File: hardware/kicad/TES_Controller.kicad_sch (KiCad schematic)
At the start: 81 parts, among them CN1 B2PS-VH, CN2 S4B-XH-A, CN3 DG381-3.5-02P-14-00A, CN5 DG381-3.5-02P-14-00A, CN6 DG381-3.5-02P-14-00A, Q1 AO3400A, Q2 AO3400A, Q3 AO3400A, Q4 AO3401A, U1 ESP32-S3-WROOM-1, U10 DG301-5.0-02P-14-00A, U12 TJA1051T_3_1J, U5 ADS1115IDGSR, U6 AMS1117-3.3, U8 LMZM23601V5SILR

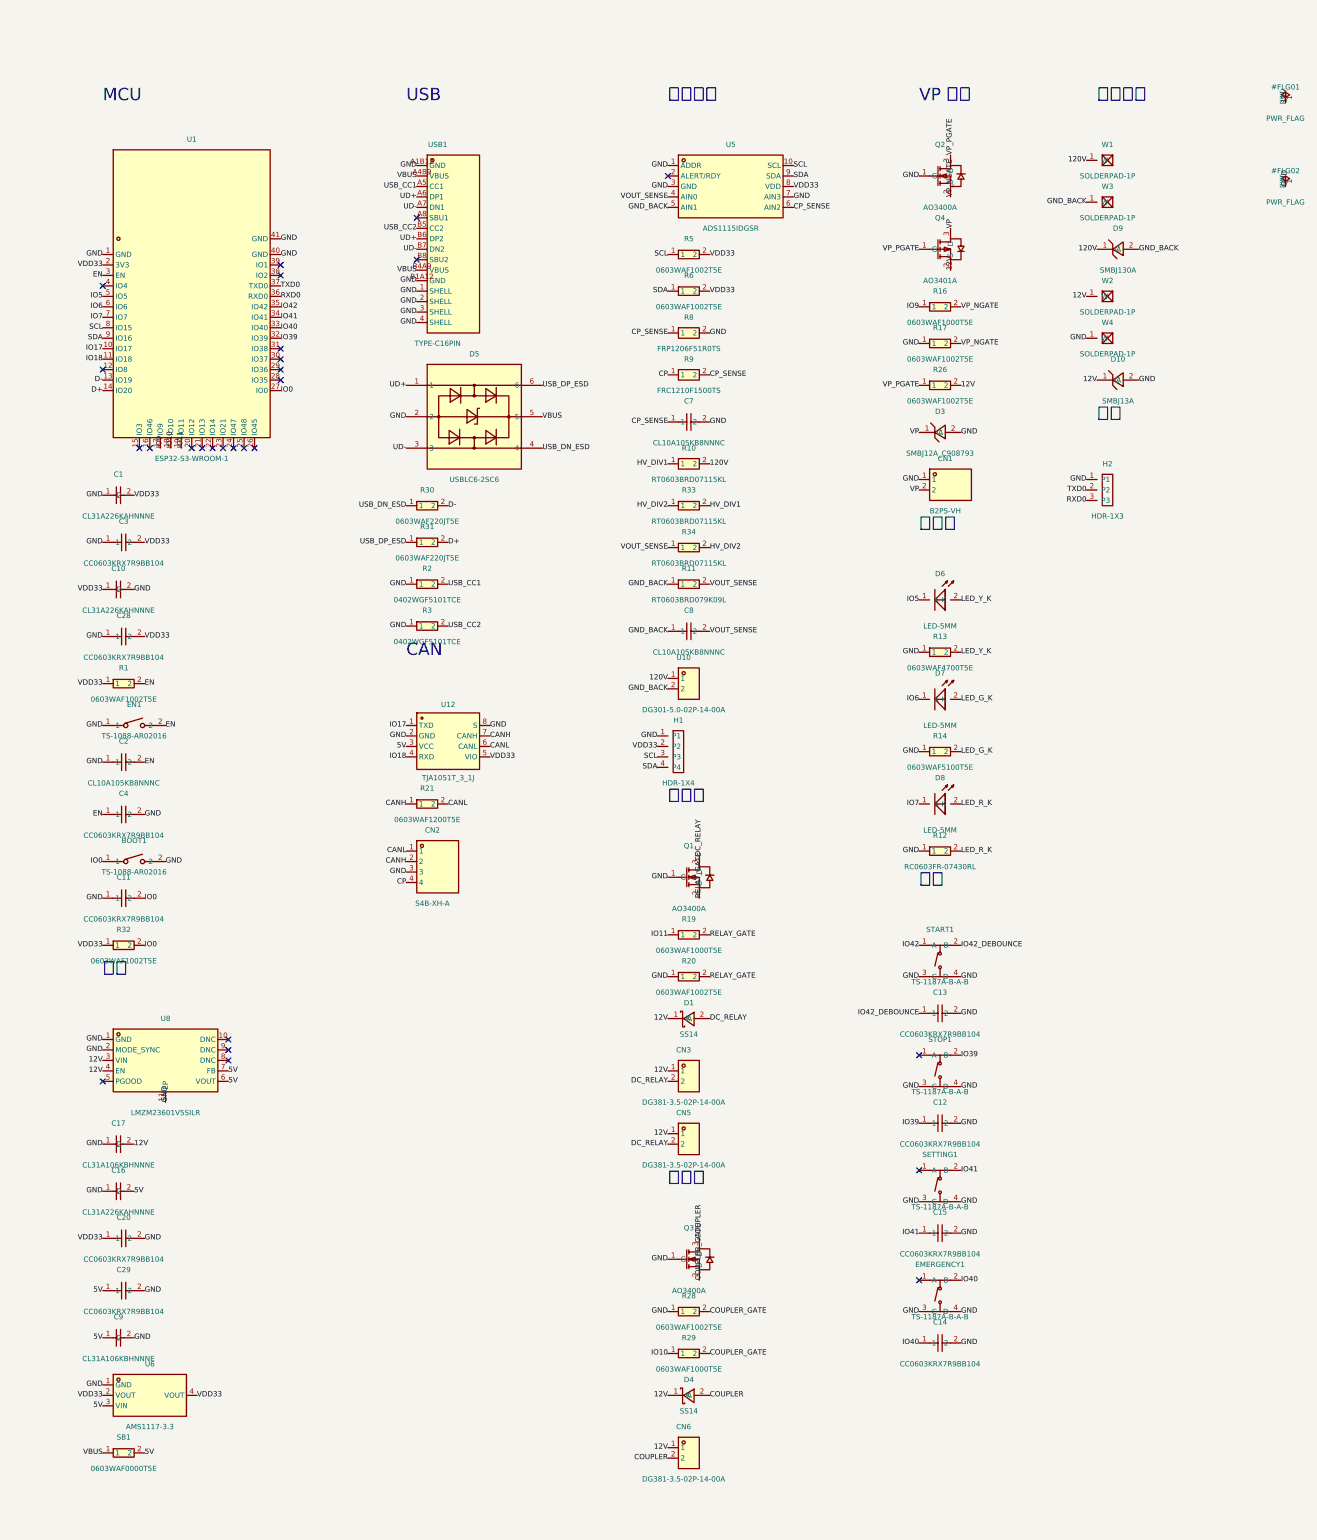
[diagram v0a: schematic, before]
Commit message: Draw the schematic with ground symbols and wires, not only labels
Chris found the schematic hard to read, and he is right: every pin carried a
net label and nothing was drawn as a connection, so a series chain looked
like three unrelated resistors sitting near each other. That was the cost of
generating it — 253 connections verified against the source, none of them
legible.

Two changes get most of it back.

Ground and supply pins become symbols instead of labels. Of 238 labels, 114
were power nets and 73 of those were GND alone; "this pin goes to ground" is
now a shape rather than a word. GND and GND_BACK are drawn differently on
purpose — the 120 V return is a separate node on the board, joined only
through the module's wiring, and one symbol for both would say otherwise.

Series chains are detected and laid out in a row with real wires between
them: the divider R34-R33-R10 and the three LED-and-resistor pairs. Chain
order comes from which side each pin sits on, so every link is a straight
horizontal line — the divider is detected as R10-R33-R34 but drawn in
reverse, because R10's connection is on its left.

Labels 232 to 119, with 115 wires and 110 power symbols.

Three things that had to be got right:

- Power symbols must be named exactly as the nets are. KiCad takes the net
  name from the symbol, so calling one +12V renames the whole net and the
  board's netlist with it.
- The stub between pin and symbol runs outward along the pin, not downward.
  At 2.54 mm it equals the symbol pin pitch, so a downward stub landed on
  the neighbouring pin and wired three no-connect pins to +12V.
- Wiring a net does not remove the need for a label on it. Dropping both
  left KiCad to auto-name the node Net-(R10-Pad1), which no longer matches
  HV_DIV1 on the board. One label per wired net keeps the name.

Netlist still verifies at 230 connections with zero difference, ERC clean,
and the board is untouched.

Co-Authored-By: Claude Opus 5 <noreply@anthropic.com>
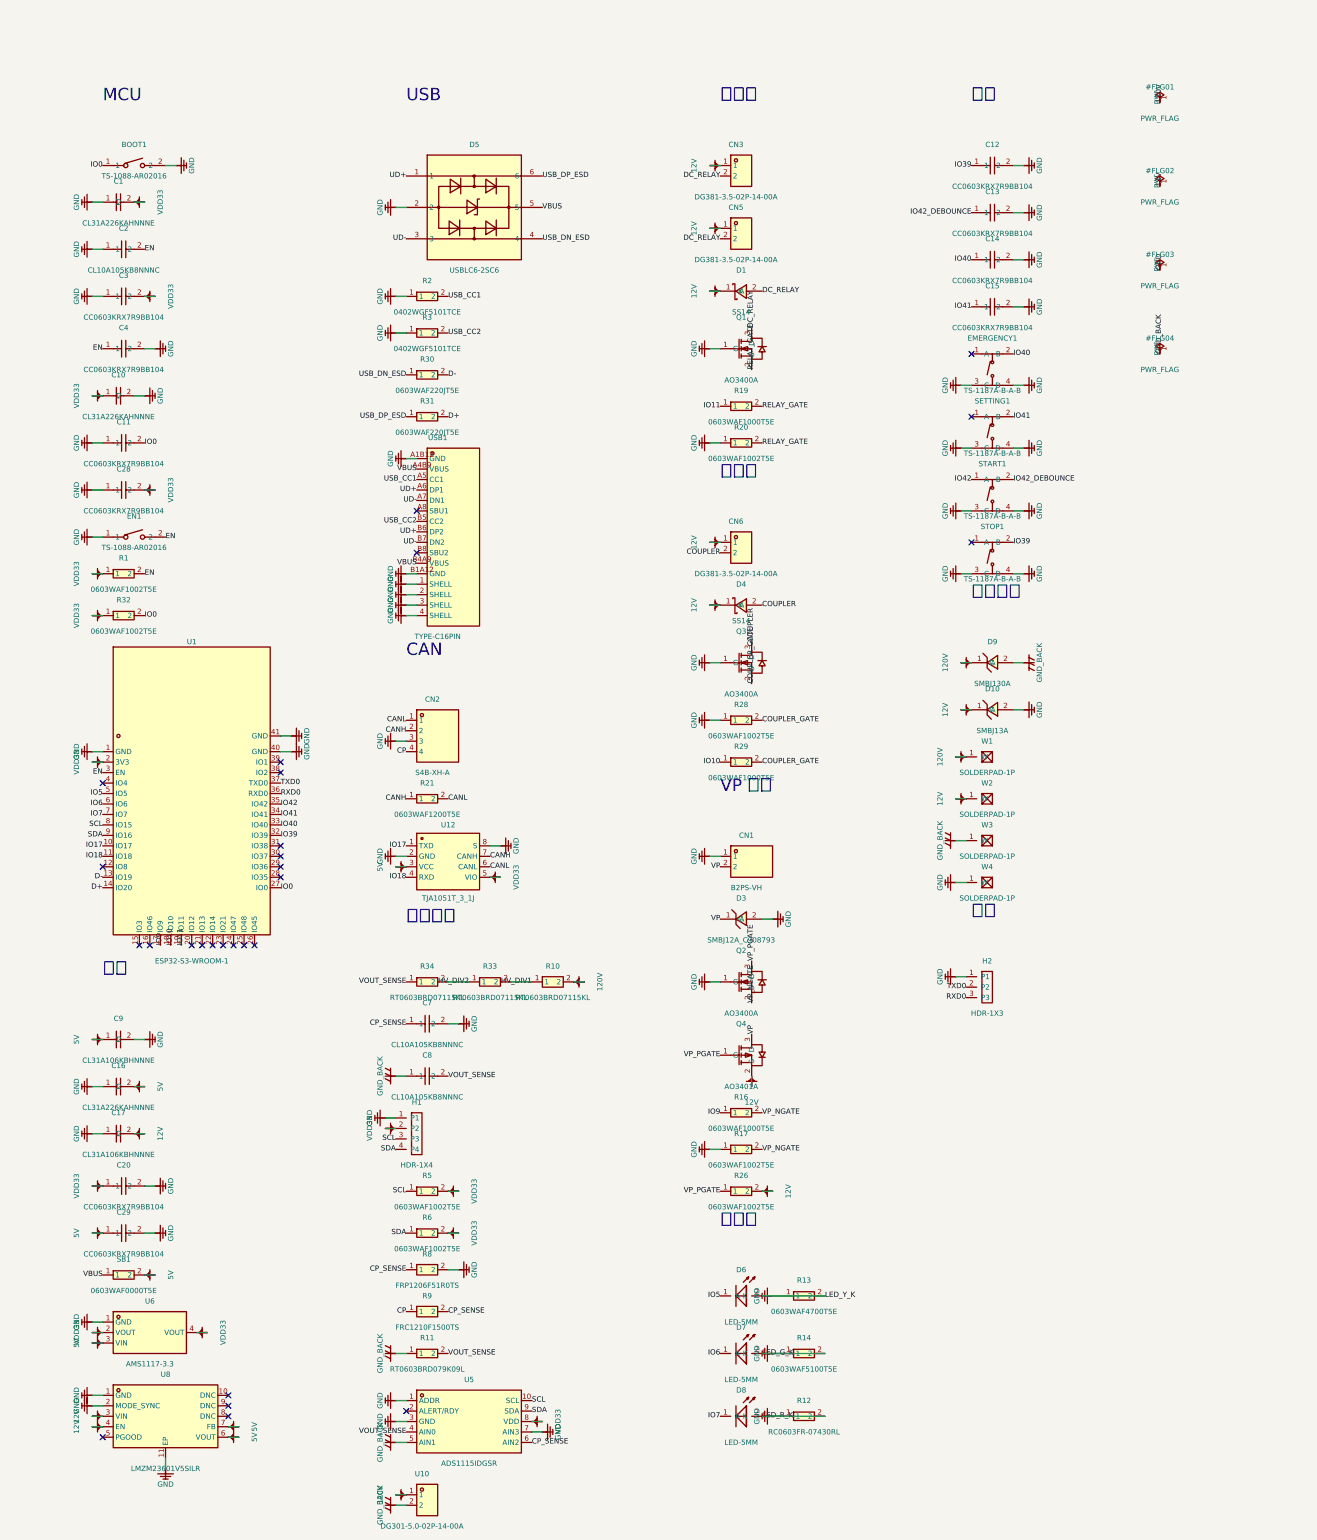
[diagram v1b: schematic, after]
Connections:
- net LED_G_K is gone; now on net GND: D7.2 (K), R14.2
- net LED_R_K is gone; now on net GND: D8.2 (K), R12.2
- net LED_Y_K is gone; now on net GND: D6.2 (K), R13.2

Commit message: Redraw the schematic the way it was drawn in EasyEDA
The generated schematic was correct but unreadable — everything was
arranged by the generator, so nothing sat where the author left it.
This rebuilds it from the original .esch: the same 73 components at the
same coordinates, the same 12 block titles and grouping boxes, the same
wires.

Getting the pins to land took working out what easyeda2kicad actually
does, which is: nothing. It copies EasyEDA's pin coordinates straight
into the KiCad symbol library, and KiCad's library Y axis points the
other way — so every symbol comes out upside down. tools/easyeda_symbols.py
checks this pin by pin against the original project file (25 of 25
symbols match with Y untouched, none negated), and the fix is to place
each symbol mirrored and rotated 180° + its original angle. KiCad
rotates before it mirrors; assuming the other order silently swaps pads
1 and 2 on every part rotated 90°, which reads as a plausible netlist.

Two things the original drawing does not tell you, both found by
comparing against the netlist rather than by eye:

* The library symbol is not always the symbol that was drawn. Q1-Q3 use
  AO3400A-MS, whose pins 1 and 2 are the reverse of the AO3400A the BOM
  points at. Wire matching now uses the symbol from the drawing, and
  components whose two geometries disagree (15 of them) are wired by
  label instead — the wires would otherwise attach to the wrong pin
  number and look fine.
* A wire group that grazes one pin of a neighbouring net used to be
  named alphabetically, so R10's move to HV_DIV1 renamed the whole
  divider midpoint. It is a majority vote now.

R10 also had to move: its pin 1 sat exactly on C8 pin 2, and once V1.3
separates those nets, cutting the wire is not enough — two labels at one
coordinate is still one node.

Netlist verifies at zero difference against the EasyEDA export (230 of
230 connections), ERC is clean, and the PCB is untouched (0 DRC errors,
0 unconnected).

Co-Authored-By: Cl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
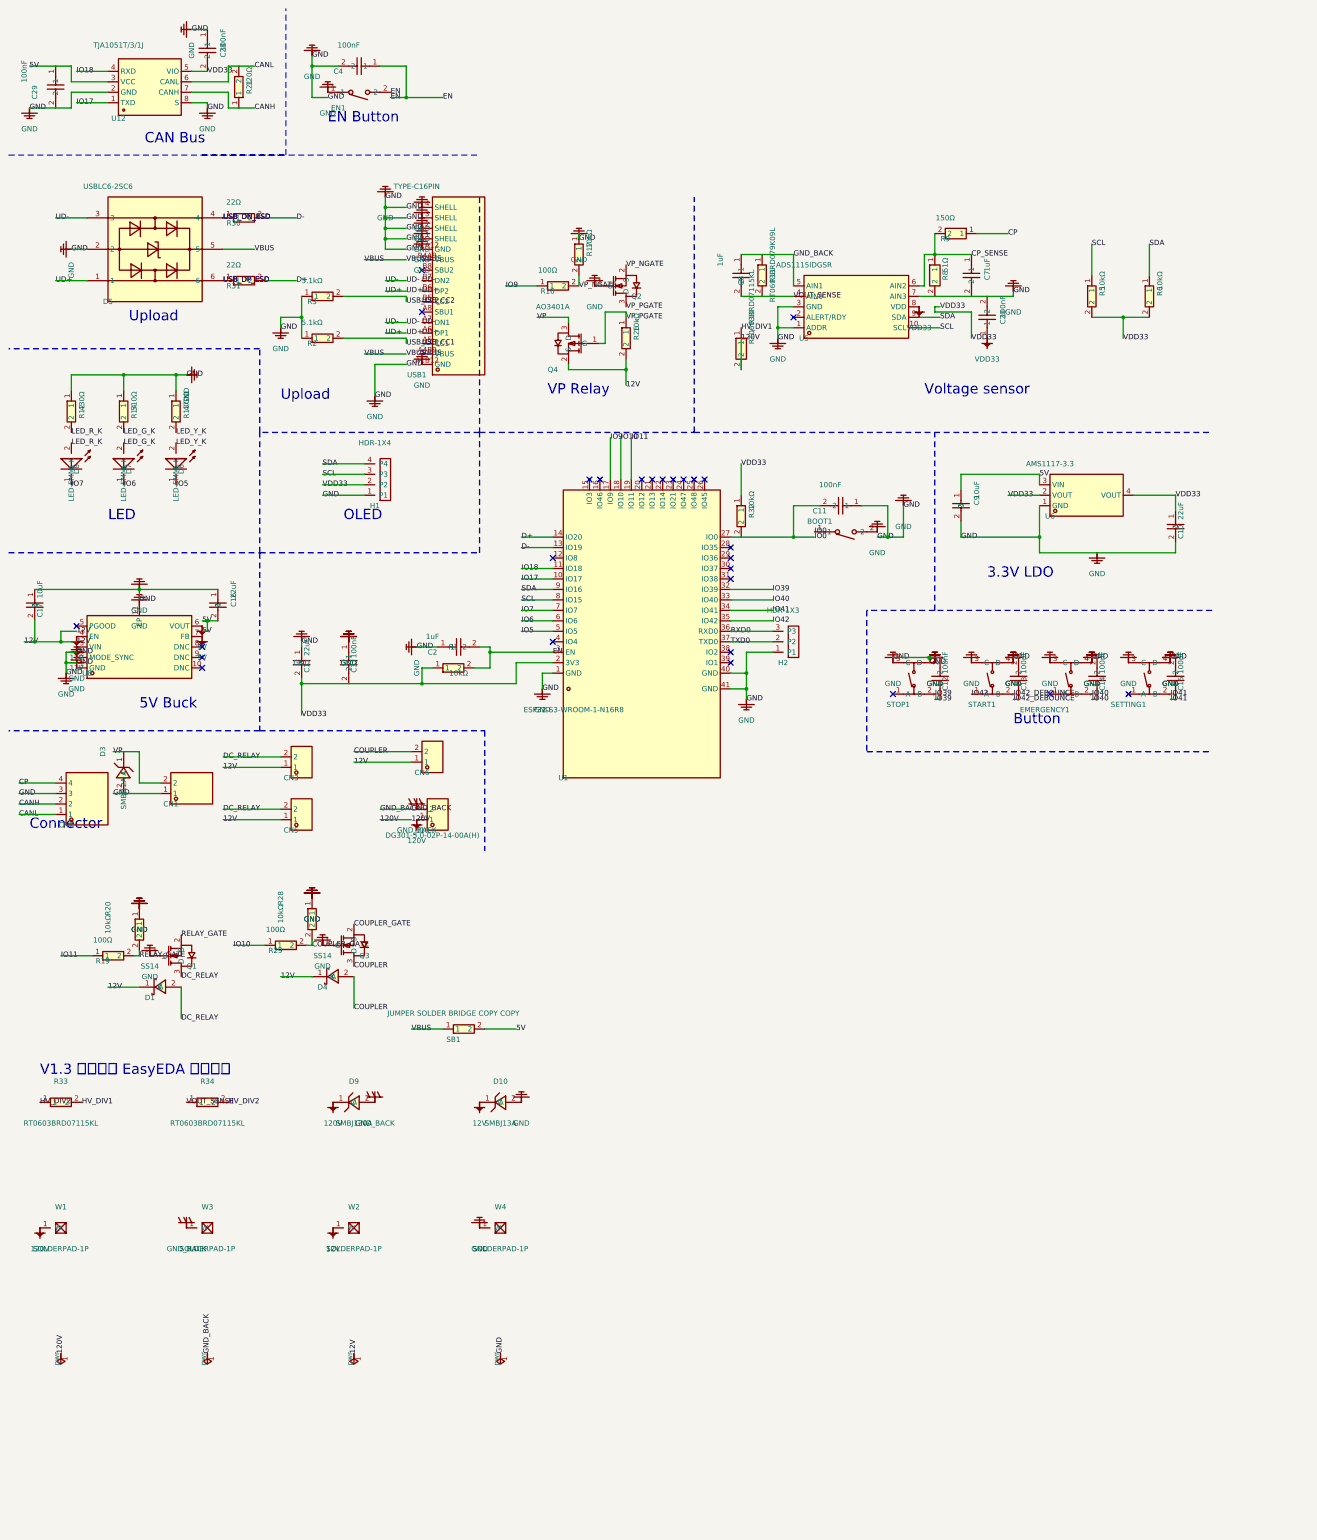
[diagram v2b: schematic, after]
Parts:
- C1, C10, C16: value CL31A226KAHNNNE -> 22uF
- C11, C12, C13, C14, C15, C20, C28, C29, C3, C4: value CC0603KRX7R9BB104 -> 100nF
- C17, C9: value CL31A106KBHNNNE -> 10uF
- C2, C7, C8: value CL10A105KB8NNNC -> 1uF
- CN1: value B2PS-VH -> B2PS-VH(LF)(SN)
- CN2: value S4B-XH-A -> S4B-XH-A(LF)(SN)
- CN3, CN5, CN6: value DG381-3.5-02P-14-00A -> DG381-3.5-02P-14-00A(H)
- D3: value SMBJ12A_C908793 -> SMBJ12A
- R1, R17, R20, R26, R28, R32, R5, R6: value 0603WAF1002T5E -> 10kΩ
- R12: value RC0603FR-07430RL -> 430Ω
- R13: value 0603WAF4700T5E -> 470Ω
- R14: value 0603WAF5100T5E -> 510Ω
- R16, R19, R29: value 0603WAF1000T5E -> 100Ω
- R2, R3: value 0402WGF5101TCE -> 5.1kΩ
- R21: value 0603WAF1200T5E -> 120Ω
- R30, R31: value 0603WAF220JT5E -> 22Ω
- R8: value FRP1206F51R0TS -> 51Ω
- R9: value FRC1210F1500TS -> 150Ω
- SB1: value 0603WAF0000T5E -> JUMPER SOLDER BRIDGE COPY COPY
- U1: value ESP32-S3-WROOM-1 -> ESP32-S3-WROOM-1-N16R8
- U10: value DG301-5.0-02P-14-00A -> DG301-5.0-02P-14-00A(H)
- U12: value TJA1051T_3_1J -> TJA1051T/3/1J
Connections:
- net GND: no longer D6.2 (K), D7.2 (K), D8.2 (K), R12.2, R13.2, R14.2
- new net LED_G_K: D7.2 (K), R14.2
- new net LED_R_K: D8.2 (K), R12.2
- new net LED_Y_K: D6.2 (K), R13.2
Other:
- note added: "3.3V LDO"
- note added: "5V Buck"
- note added: "Button"
- note added: "CAN Bus"
- note added: "Connector"
- note added: "EN Button"
- note added: "LED"
- note added: "OLED"
- note added: "Upload"
- note added: "V1.3 新增（原 EasyEDA 稿沒有）"
- note added: "VP Relay"
- note added: "Voltage sensor"
- note removed: "CAN"
- note removed: "MCU"
- note removed: "USB"
- note removed: "VP 供電"
- note removed: "其他"
- note removed: "指示燈"
- note removed: "按鍵"
- note removed: "模組接線"
- note removed: "繼電器"
- note removed: "電源"
- note removed: "電磁鎖"
- note removed: "類比量測"
